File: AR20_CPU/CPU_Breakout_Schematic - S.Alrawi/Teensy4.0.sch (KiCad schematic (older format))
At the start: 10 parts, among them SW1 SW_SPST

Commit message: 4 Layers PCB is 90% finished
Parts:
- removed MX34_Housing1: MX34_Housing, Teensy_Footprint_Library:Housing_3pins, symbol BreakoutBoardTeensy:MX34_Housing
- added C19: ?, Capacitor_SMD:C_0603_1608Metric, symbol Device:C
- added D9: 3V, Diode_SMD:D_0603_1608Metric, symbol Device:D_Zener
- added JP10: SolderJumper_2_Open, Jumper:SolderJumper-2_P1.3mm_Open_RoundedPad1.0x1.5mm, symbol Jumper:SolderJumper_2_Open
- added OpAmp1: NCV20091SQ3T2G, Teensy_Footprint_Library:SC−70_NCV20091SQ3T2G, symbol BreakoutBoardTeensy:NCV20091SQ3T2G
- added R21, R22: ?, Resistor_SMD:R_0603_1608Metric, symbol Device:R
- H4: renamed from H1; value GND -> MountingHole
- renumbered C15 to C18, H2 to H5, H3 to H6, H4 to H7, MX34 to MX1
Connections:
- net 24_A10: now also MX1.22 (Pin_22), Teensy4.0.38 (24_A10), D9.1 (K), OpAmp1.3 (IN-), OpAmp1.4 (OUT); no longer MX1.40 (Pin_40), Teensy4.0.34 (32_OUT1B)
- net 25_A11: now also MX1.24 (Pin_24), Teensy4.0.43 (25_A11); no longer MX1.39 (Pin_39), Teensy4.0.35 (30_CRX3)
- net 26_A12: now also MX1.43 (Pin_43), Teensy4.0.37 (26_A12); no longer MX1.36 (Pin_36), Teensy4.0.36 (28_RX7)
- net 27_A13: now also MX1.38 (Pin_38), Teensy4.0.42 (27_A13); no longer MX1.43 (Pin_43), Teensy4.0.37 (26_A12)
- net 28_RX7: now also MX1.36 (Pin_36), Teensy4.0.36 (28_RX7); no longer MX1.22 (Pin_22), Teensy4.0.38 (24_A10)
- net 29_TX7: now also MX1.42 (Pin_42), Teensy4.0.41 (29_TX7); no longer MX1.41 (Pin_41), Teensy4.0.39 (33_MCLK2)
- net 30_CRX3: now also MX1.39 (Pin_39), Teensy4.0.35 (30_CRX3); no longer MX1.37 (Pin_37), Teensy4.0.40 (31_CTX3)
- net 31_CTX3: now also MX1.37 (Pin_37), Teensy4.0.40 (31_CTX3); no longer MX1.42 (Pin_42), Teensy4.0.41 (29_TX7)
- net 32_OUT1B: now also MX1.40 (Pin_40), Teensy4.0.34 (32_OUT1B); no longer MX1.38 (Pin_38), Teensy4.0.42 (27_A13)
- net 33_MCLK2: now also MX1.41 (Pin_41), Teensy4.0.39 (33_MCLK2); no longer MX1.24 (Pin_24), Teensy4.0.43 (25_A11)
- net Ground: now also C19.2, D9.2 (A), OpAmp1.2 (VSS), R22.2
- net VBAT: now also R21.1
- net Vinn_5V: now also OpAmp1.5 (VDD)
- new net: C19.1, JP10.2 (B), R21.2, R22.1
- new net IN+: JP10.1 (A), OpAmp1.1 (IN+)
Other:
- moved on the sheet: BT1
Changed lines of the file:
@@
 $Descr A4 11693 8268
 encoding utf-8
-Sheet 4 6
+Sheet 6 6
 Title ""
 Date ""
@@
 Out4
 NoConn ~ 9550 4300
-Text GLabel 9550 4500 2    50   Input ~ 0
+Text GLabel 7200 4600 0    50   Input ~ 0
 26_A12
-Text GLabel 9550 4400 2    50   Input ~ 0
+Text GLabel 9550 4600 2    50   Input ~ 0
 24_A10
 Text GLabel 9550 4200 2    50   Input ~ 0
@@
 AR Path="/5DFC9DF7" Ref="Teensy4.?"  Part="1"
 AR Path="/5DFC2DB2/5DFC9DF7" Ref="Teensy4.0"  Part="1"
-F 0 "Teensy4.0" H 8425 4425 50  0000 C CNN
+AR Path="/5DE8C5CE/5DFC9DF7" Ref="Teensy4.1"  Part="1"
+F 0 "Teensy4.1" H 8425 4425 50  0000 C CNN
 F 1 "Teensy_pins" H 8425 4334 50  0000 C CNN
 F 2 "Teensy_Footprint_Library:Teensy_40_footprint" H 9150 3500 50  0001 C CNN
@@
 Wire Wire Line
 	9550 3000 9450 3000
-Text GLabel 9550 4600 2    50   Input ~ 0
+Text GLabel 9550 4500 2    50   Input ~ 0
 28_RX7
-Text GLabel 9550 4700 2    50   Input ~ 0
+Text GLabel 7200 4500 0    50   Input ~ 0
 30_CRX3
-Text GLabel 9550 4800 2    50   Input ~ 0
+Text GLabel 9550 4400 2    50   Input ~ 0
 32_OUT1B
 Wire Wire Line
@@
 Text GLabel 7200 3900 0    50   Input ~ 0
 10_CS
-Text GLabel 7200 4900 0    50   Input ~ 0
+Text GLabel 7200 4700 0    50   Input ~ 0
 33_MCLK2
-Text GLabel 7200 4800 0    50   Input ~ 0
+Text GLabel 9550 4700 2    50   Input ~ 0
 31_CTX3
-Text GLabel 7200 4700 0    50   Input ~ 0
+Text GLabel 7200 4800 0    50   Input ~ 0
 29_TX7
-Text GLabel 7200 4600 0    50   Input ~ 0
+Text GLabel 9550 4800 2    50   Input ~ 0
 27_A13
-Text GLabel 7200 4500 0    50   Input ~ 0
+Text GLabel 7200 4900 0    50   Input ~ 0
 25_A11
 Text GLabel 7200 3800 0    50   Input ~ 0
@@
 L Device:Battery_Cell BT1
 U 1 1 5DFDECDE
-P 7600 1150
-F 0 "BT1" H 7350 1250 50  0000 L CNN
-F 1 "3V cell coin" H 7000 1150 50  0000 L CNN
-F 2 "Battery:BatteryHolder_Keystone_3034_1x20mm" V 7600 1210 50  0001 C CNN
-F 3 "~" V 7600 1210 50  0001 C CNN
-	1    7600 1150
-	0    -1   -1   0
+P 10150 1350
+F 0 "BT1" H 10300 1500 50  0000 L CNN
+F 1 "3V cell coin" H 10250 1350 50  0000 L CNN
+F 2 "Battery:BatteryHolder_Keystone_3034_1x20mm" V 10150 1410 50  0001 C CNN
+F 3 "~" V 10150 1410 50  0001 C CNN
+	1    10150 1350
+	1    0    0    -1
 $EndComp
-Wire Wire Line
-	7350 1150 7400 1150
 $Comp
 L Switch:SW_SPST SW1
@@
 Text GLabel 6300 1650 3    50   Input ~ 0
 Ground
-Wire Wire Line
-	7700 1150 7700 1200
 Text GLabel 6300 1000 1    50   Input ~ 0
 ON_OFF
 Wire Wire Line
 	6300 1250 6300 1000
-Text GLabel 7350 1150 1    50   Input ~ 0
+Text GLabel 10150 900  1    50   Input ~ 0
 VBAT
 $Bitmap
@@
 Wire Wire Line
 	4600 3900 4500 3900
-Text GLabel 4400 4900 0    50   Input ~ 0
+Text GLabel 4500 3900 0    50   Input ~ 0
 24_A10
-Text GLabel 4400 4500 0    50   Input ~ 0
+Text GLabel 4400 5200 0    50   Input ~ 0
 26_A12
-Text GLabel 4500 3900 0    50   Input ~ 0
+Text GLabel 4400 4500 0    50   Input ~ 0
 28_RX7
-Text GLabel 4400 4000 0    50   Input ~ 0
+Text GLabel 4400 5000 0    50   Input ~ 0
 33_MCLK2
-Text GLabel 4400 5100 0    50   Input ~ 0
+Text GLabel 4400 4600 0    50   Input ~ 0
 31_CTX3
-Text GLabel 4400 5000 0    50   Input ~ 0
+Text GLabel 4400 5100 0    50   Input ~ 0
 29_TX7
-Text GLabel 4400 5200 0    50   Input ~ 0
+Text GLabel 4400 4700 0    50   Input ~ 0
 27_A13
-Text GLabel 4400 4800 0    50   Input ~ 0
+Text GLabel 4400 4000 0    50   Input ~ 0
 25_A11
 Text GLabel 4500 3600 0    50   Input ~ 0
@@
 Wire Wire Line
 	4600 5800 4400 5800
-Text GLabel 4400 4600 0    50   Input ~ 0
+Text GLabel 4400 4800 0    50   Input ~ 0
 30_CRX3
-Text GLabel 4400 4700 0    50   Input ~ 0
+Text GLabel 4400 4900 0    50   Input ~ 0
 32_OUT1B
-$Comp
-L BreakoutBoardTeensy:MX34_Housing MX34_Housing1
-U 1 1 5DFDED28
-P 4350 1250
-F 0 "MX34_Housing1" H 4475 1775 50  0000 C CNN
-F 1 "MX34_Housing" H 4475 1684 50  0000 C CNN
-F 2 "Teensy_Footprint_Library:Housing_3pins" H 4350 1250 50  0001 C CNN
-F 3 "" H 4350 1250 50  0001 C CNN
-	1    4350 1250
-	1    0    0    -1
-$EndComp
 Text GLabel 4500 3800 0    50   Input ~ 0
 3V3
@@
 Text GLabel 4400 6200 0    50   Input ~ 0
 12V_IN
-Text GLabel 7700 1200 3    50   Input ~ 0
-Ground
-Text GLabel 4450 1450 3    50   Input ~ 0
+Text GLabel 10150 1650 3    50   Input ~ 0
 Ground
 Text GLabel 4400 6100 0    50   Input ~ 0
 Ground
-Wire Wire Line
-	4350 1150 4450 1150
-Wire Wire Line
-	4350 1050 4450 1050
-Wire Wire Line
-	4350 950  4450 950
-Wire Wire Line
-	4450 1150 4450 1450
-Connection ~ 4450 1150
-Wire Wire Line
-	4450 1150 4550 1150
-Wire Wire Line
-	4450 1150 4450 1050
-Connection ~ 4450 1050
-Wire Wire Line
-	4450 1050 4550 1050
-Wire Wire Line
-	4450 950  4450 1050
-Connection ~ 4450 950
-Wire Wire Line
-	4450 950  4550 950
 $Comp
-L Device:C C15
+L Device:C C18
 U 1 1 5DFDED4D
 P 4500 6350
-F 0 "C15" H 4615 6396 50  0000 L CNN
+F 0 "C18" H 4615 6396 50  0000 L CNN
 F 1 "10u" H 4615 6305 50  0000 L CNN
 F 2 "Capacitor_SMD:C_0603_1608Metric" H 4538 6200 50  0001 C CNN
@@
 	4500 6500 4500 6650
 $Comp
-L Mechanical:MountingHole H1
+L Mechanical:MountingHole H4
 U 1 1 5DFDED57
 P 9050 5400
-F 0 "H1" H 9150 5446 50  0000 L CNN
-F 1 "GND" H 9150 5355 50  0000 L CNN
+F 0 "H4" H 9150 5446 50  0000 L CNN
+F 1 "MountingHole" H 9150 5355 50  0000 L CNN
 F 2 "MountingHole:MountingHole_2.5mm_Pad" H 9050 5400 50  0001 C CNN
 F 3 "~" H 9050 5400 50  0001 C CNN
@@
 $EndComp
 $Comp
-L Mechanical:MountingHole H2
+L Mechanical:MountingHole H5
 U 1 1 5DFDED5D
 P 9050 5650
-F 0 "H2" H 9150 5696 50  0000 L CNN
+F 0 "H5" H 9150 5696 50  0000 L CNN
 F 1 "MountingHole" H 9150 5605 50  0000 L CNN
 F 2 "MountingHole:MountingHole_2.5mm_Pad" H 9050 5650 50  0001 C CNN
@@
 $EndComp
 $Comp
-L Mechanical:MountingHole H3
+L Mechanical:MountingHole H6
 U 1 1 5DFDED63
 P 9050 5900
-F 0 "H3" H 9150 5946 50  0000 L CNN
+F 0 "H6" H 9150 5946 50  0000 L CNN
 F 1 "MountingHole" H 9150 5855 50  0000 L CNN
 F 2 "MountingHole:MountingHole_2.5mm_Pad" H 9050 5900 50  0001 C CNN
@@
 $EndComp
 $Comp
-L Mechanical:MountingHole H4
+L Mechanical:MountingHole H7
 U 1 1 5DFDED69
 P 9050 6200
-F 0 "H4" H 9150 6246 50  0000 L CNN
+F 0 "H7" H 9150 6246 50  0000 L CNN
 F 1 "MountingHole" H 9150 6155 50  0000 L CNN
 F 2 "MountingHole:MountingHole_2.5mm_Pad" H 9050 6200 50  0001 C CNN
@@
 $EndComp
 $Comp
-L teensy4_header_breakout-cache:MX34_36_pins MX34
+L teensy4_header_breakout-cache:MX34_36_pins MX1
 U 1 1 5DFDED6F
 P 4800 4400
-F 0 "MX34" H 3400 4450 50  0000 L CNN
+F 0 "MX1" H 3400 4450 50  0000 L CNN
 F 1 "MX34_36_pins" H 3300 4600 50  0000 L CNN
 F 2 "Teensy_Footprint_Library:Connector_MX34_36pins" H 4800 4400 50  0001 C CNN
@@
 Text GLabel 4500 3700 0    50   Input ~ 0
 3.3V
+$Comp
+L Device:R R21
+U 1 1 5DE96DA3
+P 9750 1100
+F 0 "R21" H 9820 1146 50  0000 L CNN
+F 1 "?" H 9820 1055 50  0000 L CNN
+F 2 "Resistor_SMD:R_0603_1608Metric" V 9680 1100 50  0001 C CNN
+F 3 "~" H 9750 1100 50  0001 C CNN
+	1    9750 1100
+	1    0    0    -1
+$EndComp
+$Comp
+L Device:R R22
+U 1 1 5DE9741A
+P 9750 1450
+F 0 "R22" H 9820 1496 50  0000 L CNN
+F 1 "?" H 9820 1405 50  0000 L CNN
+F 2 "Resistor_SMD:R_0603_1608Metric" V 9680 1450 50  0001 C CNN
+F 3 "~" H 9750 1450 50  0001 C CNN
+	1    9750 1450
+	1    0    0    -1
+$EndComp
+Wire Wire Line
+	10150 1150 10150 950
+Wire Wire Line
+	10150 1450 10150 1600
+Wire Wire Line
+	9750 1300 9750 1250
+Wire Wire Line
+	9750 950  10150 950
+Connection ~ 10150 950
+Wire Wire Line
+	10150 950  10150 900
+Wire Wire Line
+	9750 1600 10150 1600
+Connection ~ 10150 1600
+Wire Wire Line
+	10150 1600 10150 1650
+Connection ~ 9750 1250
+$Comp
+L Jumper:SolderJumper_2_Open JP10
+U 1 1 5DEBD2EA
+P 9200 1250
+F 0 "JP10" H 9200 1350 50  0000 C CNN
+F 1 "SolderJumper_2_Open" H 9250 1400 50  0000 C CNN
+F 2 "Jumper:SolderJumper-2_P1.3mm_Open_RoundedPad1.0x1.5mm" H 9200 1250 50  0001 C CNN
+F 3 "~" H 9200 1250 50  0001 C CNN
+	1    9200 1250
+	1    0    0    -1
+$EndComp
+Wire Wire Line
+	9050 1250 8900 1250
+Text GLabel 7600 1700 0    50   Input ~ 0
+24_A10
+$Comp
+L Device:C C19
+U 1 1 5DEC35AF
+P 9500 1450
+F 0 "C19" H 9250 1500 50  0000 L CNN
+F 1 "?" H 9250 1350 50  0000 L CNN
+F 2 "Capacitor_SMD:C_0603_1608Metric" H 9538 1300 50  0001 C CNN
+F 3 "~" H 9500 1450 50  0001 C CNN
+	1    9500 1450
+	1    0    0    -1
+$EndComp
+Wire Wire Line
+	9500 1300 9500 1250
+Connection ~ 9500 1250
+Wire Wire Line
+	9500 1250 9350 1250
+Wire Wire Line
+	9500 1250 9750 1250
+Text GLabel 9500 1650 3    50   Input ~ 0
+Ground
+Wire Wire Line
+	9500 1600 9500 1650
+Text GLabel 8950 900  1    50   Input ~ 0
+Vinn_5V
+Text GLabel 7600 1350 0    50   Input ~ 0
+Ground
+$Comp
+L BreakoutBoardTeensy:NCV20091SQ3T2G OpAmp1
+U 1 1 5DEC29A5
+P 8350 1900
+F 0 "OpAmp1" H 8300 3065 50  0000 C CNN
+F 1 "NCV20091SQ3T2G" H 8300 2974 50  0000 C CNN
+F 2 "Teensy_Footprint_Library:SC−70_NCV20091SQ3T2G" H 8350 1900 50  0001 C CNN
+F 3 "" H 8350 1900 50  0001 C CNN
+	1    8350 1900
+	1    0    0    -1
+$EndComp
+Text GLabel 8900 1250 3    50   Input ~ 0
+IN+
+Text GLabel 7600 1000 0    50   Input ~ 0
+IN+
+Wire Wire Line
+	7600 1700 7700 1700
+Wire Wire Line
+	7600 1350 7750 1350
+Wire Wire Line
+	7600 1000 7750 1000
+Wire Wire Line
+	8850 1700 9000 1700
+Wire Wire Line
+	8850 1000 8950 1000
+Wire Wire Line
+	8950 1000 8950 900
+Wire Wire Line
+	9000 1950 7800 1950
+Wire Wire Line
+	7700 1950 7700 1700
+Wire Wire Line
+	9000 1700 9000 1950
+Connection ~ 7700 1700
+Wire Wire Line
+	7700 1700 7750 1700
+Wire Wire Line
+	10550 2050 10550 2000
+Wire Wire Line
+	10550 2400 10550 2350
+$Comp
+L Device:D_Zener D?
+U 1 1 5DEF67C8
+P 7800 2100
+AR Path="/5DE81E30/5DEF67C8" Ref="D?"  Part="1"
+AR Path="/5DE8C5CE/5DEF67C8" Ref="D9"  Part="1"
+F 0 "D9" V 7846 2021 50  0000 R CNN
+F 1 "3V" V 7750 2000 50  0000 R CNN
+F 2 "Diode_SMD:D_0603_1608Metric" H 7800 2100 50  0001 C CNN
+F 3 "~" H 7800 2100 50  0001 C CNN
+	1    7800 2100
+	0    1    1    0
+$EndComp
+Connection ~ 7800 1950
+Wire Wire Line
+	7800 1950 7700 1950
+Text GLabel 7800 2400 0    50   Input ~ 0
+Ground
+Wire Wire Line
+	7800 2400 7800 2250
 $EndSCHEMATC

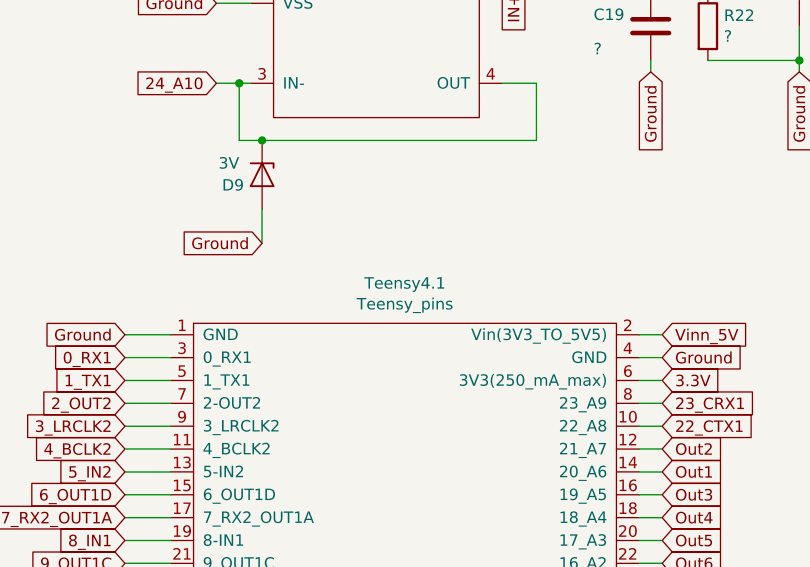
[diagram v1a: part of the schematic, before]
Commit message: Edited the Vreg  to SD
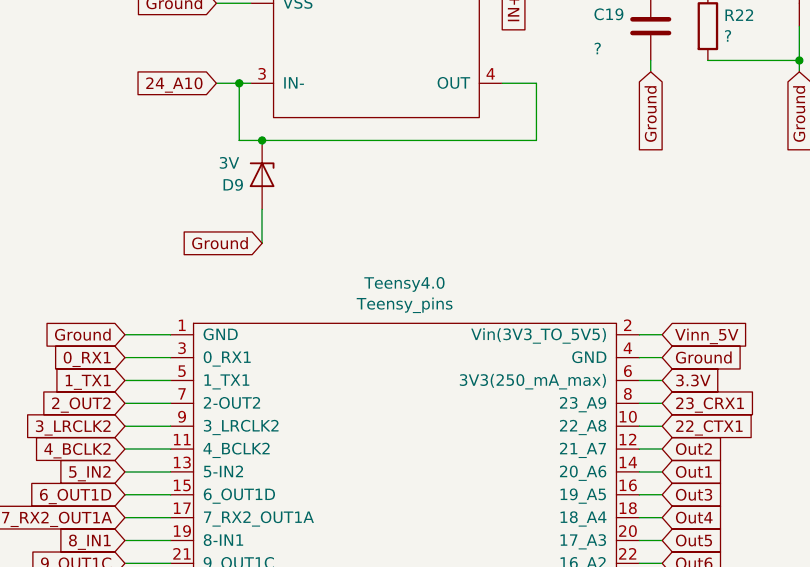
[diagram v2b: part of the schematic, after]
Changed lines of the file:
@@
 AR Path="/5DFC9DF7" Ref="Teensy4.?"  Part="1"
 AR Path="/5DFC2DB2/5DFC9DF7" Ref="Teensy4.0"  Part="1"
-AR Path="/5DE8C5CE/5DFC9DF7" Ref="Teensy4.1"  Part="1"
-F 0 "Teensy4.1" H 8425 4425 50  0000 C CNN
+AR Path="/5DE8C5CE/5DFC9DF7" Ref="Teensy4.0"  Part="1"
+F 0 "Teensy4.0" H 8425 4425 50  0000 C CNN
 F 1 "Teensy_pins" H 8425 4334 50  0000 C CNN
 F 2 "Teensy_Footprint_Library:Teensy_40_footprint" H 9150 3500 50  0001 C CNN
